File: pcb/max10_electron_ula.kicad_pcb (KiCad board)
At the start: 4 copper layers, 55 x 89 mm, 149 parts

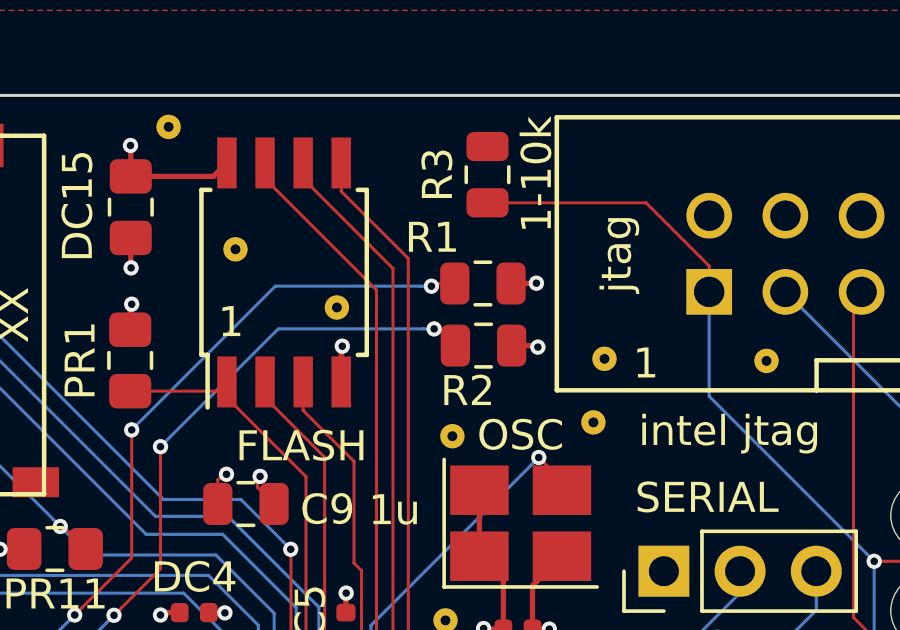
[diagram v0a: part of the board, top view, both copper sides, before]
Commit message: Finalized PR* names and renamed 10k R1/R2 to PR12/PR13 for consistency
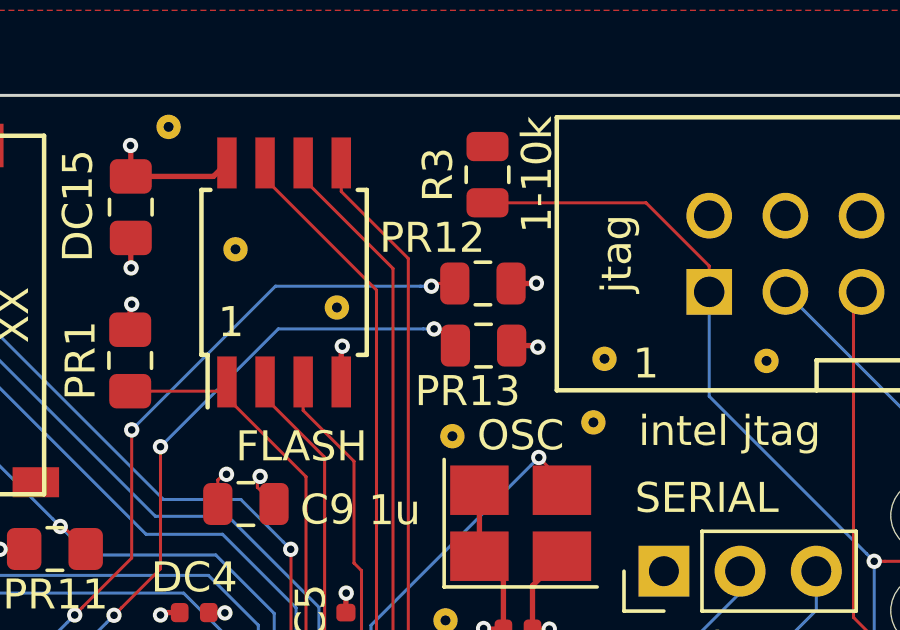
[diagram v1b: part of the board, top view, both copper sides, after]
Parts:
- AR3: value NF 10k -> 10k NF
- renumbered R1 to PR12, R2 to PR13
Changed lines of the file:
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@@
       (effects (font (size 1 1) (thickness 0.15)))
     )
-    (fp_text value "NF 10k" (at 0 1.65 270) (layer F.Fab)
+    (fp_text value "10k NF" (at 0 1.65 270) (layer F.Fab)
       (effects (font (size 1 1) (thickness 0.15)))
     )
@@
     (tags resistor)
     (attr smd)
-    (fp_text reference R1 (at -1.6875 -1.52) (layer F.SilkS)
+    (fp_text reference PR12 (at -1.6875 -1.52) (layer F.SilkS)
       (effects (font (size 1 1) (thickness 0.15)))
     )
@@
     (tags resistor)
     (attr smd)
-    (fp_text reference R2 (at -0.5275 1.52) (layer F.SilkS)
-      (effects (font (size 1 1) (thickness 0.15)))
-    )
+    (fp_text reference PR13 (at -0.5275 1.52) (layer F.SilkS)
+      (effects (font (size 1 1) (thickness 0.15)))
+    )

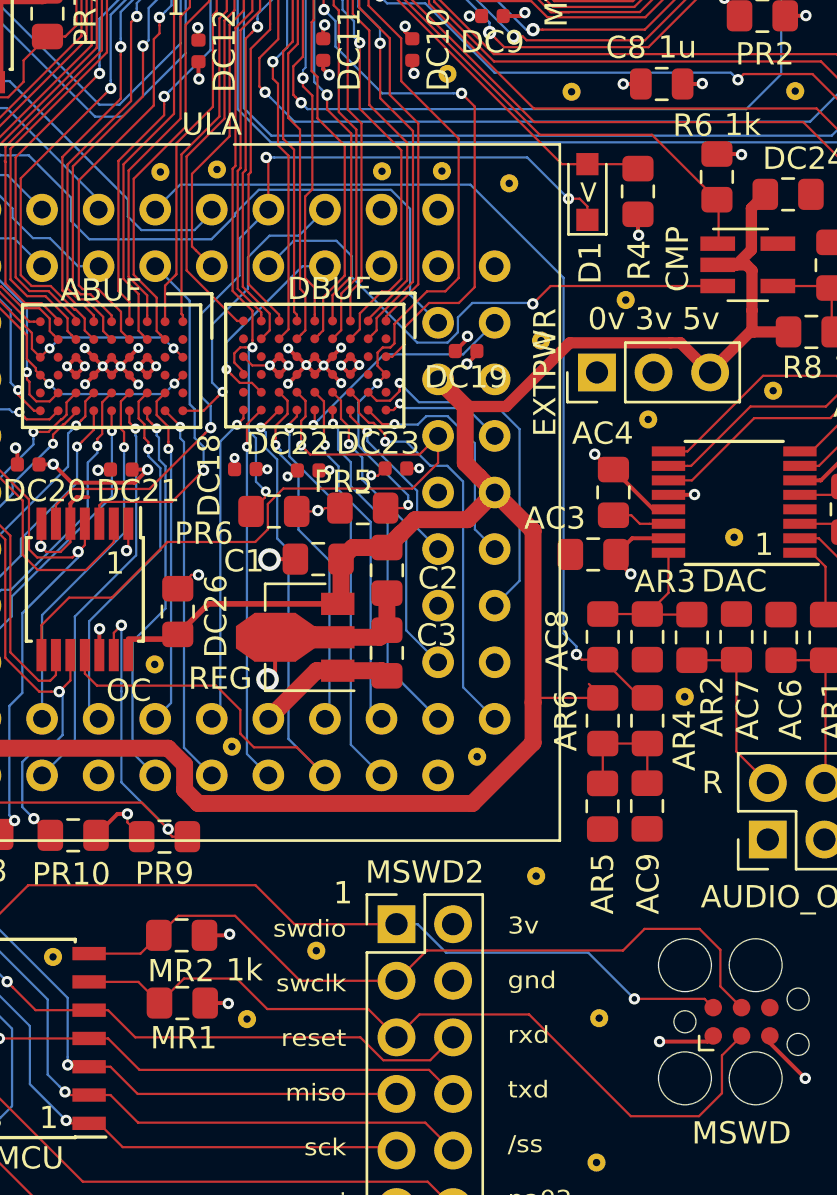
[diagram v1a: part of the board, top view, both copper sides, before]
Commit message: Renamed R4 to PR14 and MR1 to PR15 for consistency
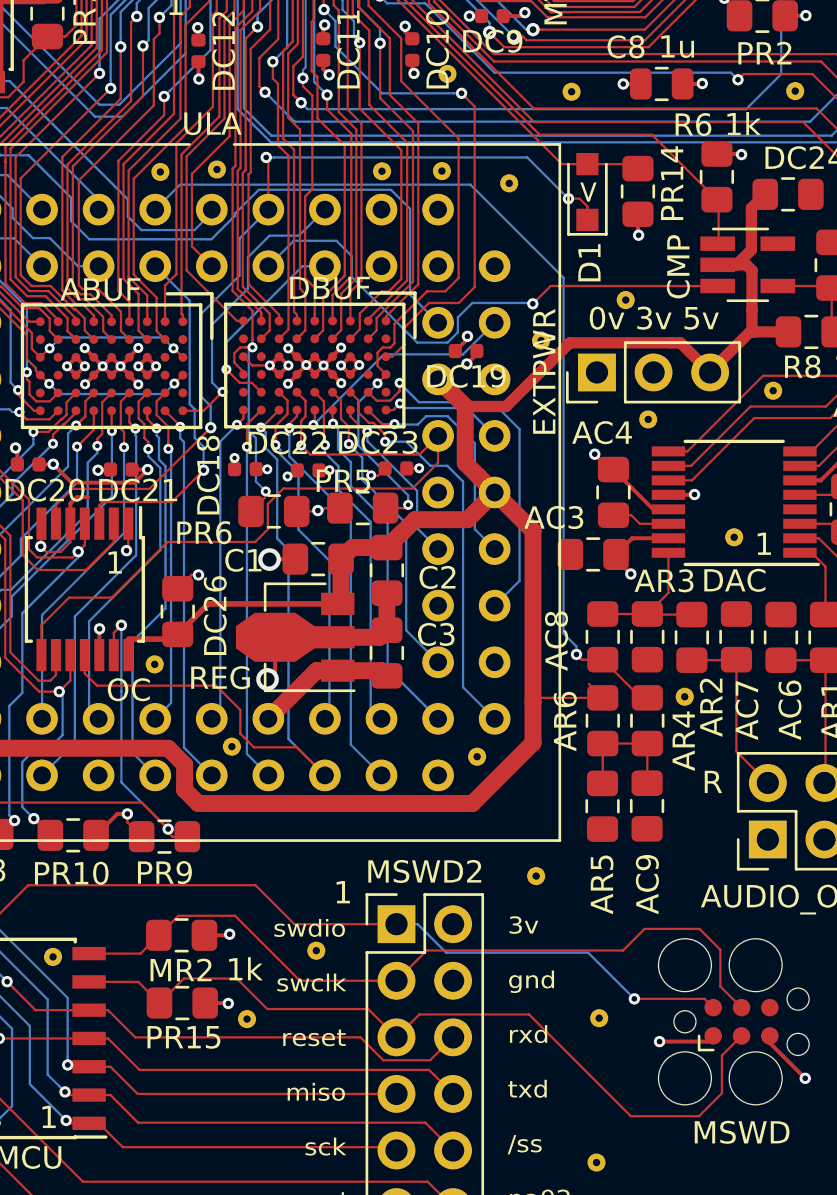
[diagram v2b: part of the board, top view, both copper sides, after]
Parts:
- renumbered R4 to PR14, MR1 to PR15
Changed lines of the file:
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@@
     (tags "resistor handsolder")
     (attr smd)
-    (fp_text reference R4 (at -3.095 0.06 90) (layer F.SilkS)
+    (fp_text reference PR14 (at 0.345 1.57 90) (layer F.SilkS)
       (effects (font (size 1 1) (thickness 0.15)))
     )
@@
     (tags "SOT-23-5 hand-soldering")
     (attr smd)
-    (fp_text reference CMP (at -3.15 -0.26 90) (layer F.SilkS)
+    (fp_text reference CMP (at -3.08 0.1 90) (layer F.SilkS)
       (effects (font (size 1 1) (thickness 0.15)))
     )
@@
     (tags "resistor handsolder")
     (attr smd)
-    (fp_text reference MR1 (at 0.065 1.57) (layer F.SilkS)
-      (effects (font (size 1 1) (thickness 0.15)))
-    )
+    (fp_text reference PR15 (at 0.065 1.57) (layer F.SilkS)
+      (effects (font (size 1 1) (thickness 0.15)))
+    )

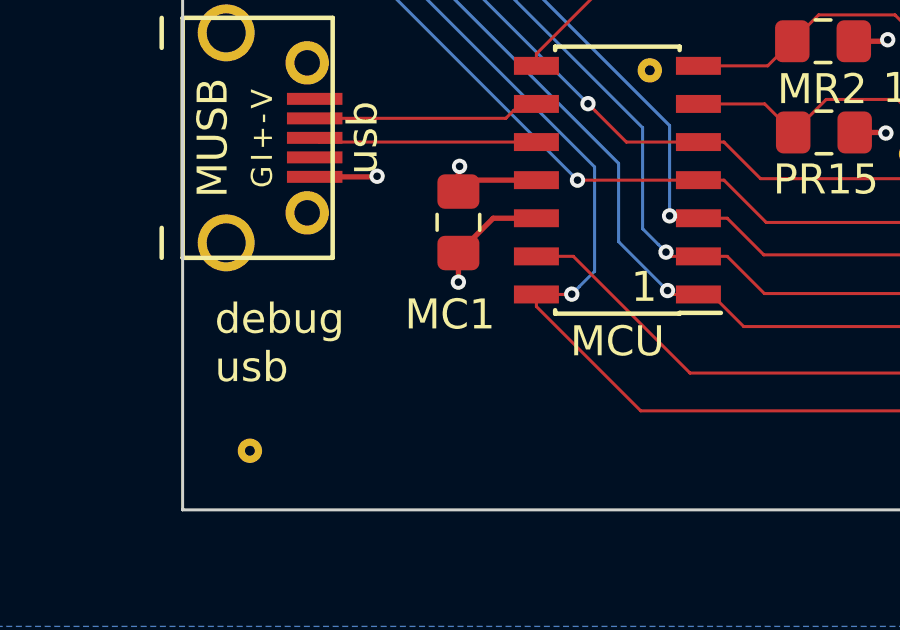
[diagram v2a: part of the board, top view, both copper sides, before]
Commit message: Renamed MC1 to DC27
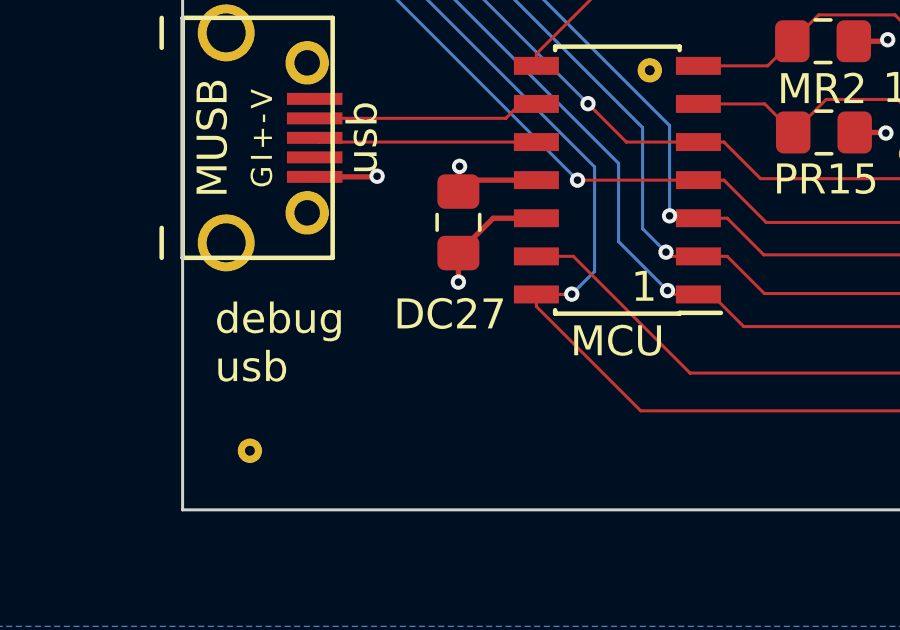
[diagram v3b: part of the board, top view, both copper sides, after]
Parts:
- renumbered MC1 to DC27
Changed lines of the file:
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@@
     (tags "capacitor handsolder")
     (attr smd)
-    (fp_text reference MC1 (at 3.075 0.28) (layer F.SilkS)
+    (fp_text reference DC27 (at 3.075 0.28) (layer F.SilkS)
       (effects (font (size 1 1) (thickness 0.15)))
     )

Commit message: Update version to v2
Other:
- board text added: ""Ultimate Electron Upgrade" http://myelin.nz/elkula v2 - 2019-??-??"
- board text removed: ""Ultimate Electron Upgrade" http://myelin.nz/elkula v1 - 2019-05-15"
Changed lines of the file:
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@@
     (effects (font (size 1 1) (thickness 0.2)) (justify left))
   )
-  (gr_text "\"Ultimate Electron Upgrade\"\nhttp://myelin.nz/elkula\nv1 - 2019-05-15" (at 150.9 73.08 90) (layer F.SilkS)
+  (gr_text "\"Ultimate Electron Upgrade\"\nhttp://myelin.nz/elkula\nv2 - 2019-??-??" (at 150.9 73.08 90) (layer F.SilkS)
     (effects (font (size 1 1) (thickness 0.2)))
   )
